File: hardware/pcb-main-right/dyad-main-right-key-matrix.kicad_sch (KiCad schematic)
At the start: 74 parts, among them SW1 SW_Push, SW10 SW_Push, SW11 SW_Push, SW12 SW_Push, SW13 SW_Push, SW14 SW_Push, SW15 SW_Push, SW16 SW_Push, SW17 SW_Push, SW18 SW_Push, SW19 SW_Push, SW2 SW_Push, SW20 SW_Push, SW21 SW_Push, SW22 SW_Push, SW23 SW_Push, SW24 SW_Push, SW25 SW_Push, SW26 SW_Push, SW27 SW_Push, SW28 SW_Push, SW29 SW_Push, SW3 SW_Push, SW30 SW_Push, SW31 SW_Push, SW32 SW_Push, SW33 SW_Push, SW34 SW_Push, SW35 SW_Push, SW36 SW_Push, SW37 SW_Push, SW4 SW_Push, SW5 SW_Push, SW6 SW_Push, SW7 SW_Push, SW8 SW_Push, SW9 SW_Push

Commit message: Move the right half's thumb keys onto their physical columns, and route it
The two rotated thumb keys were wired to COL5 and COL6 while sitting
physically leftmost on the board, because KLE puts rotated keys in their own
rows and they were numbered last. COL5 and COL6 therefore had to reach ~92 mm
across the board to find them. Relabelled 4,5 -> 4,0 and 4,6 -> 4,1 in the
KLE (with the five straight bottom-row keys shifted up to 4,2..4,6 to make
room) and regenerated: SW31 is now COL0 at x=46.23 and SW32 is COL1 at
x=68.98, both directly below the columns they belong to.

Also carries the hand routing done on top of that regeneration: all five ROW
nets and COL0-COL5, COL7 complete, 118 -> 234 segments. Unconnected 221 -> 183.
The remainder is 146 VCC/GND (no copper pours yet), 36 LED DOUT chain, and one
COL6 hop from SW22's pad to the end of its track.

Two errors on COL3 predate the routing and come from kbplacer's generated
traces: 0.1386 mm to LED26's cutout, and 0.197 mm to SW26's NPTH pad. The
nudge pass declined the first rather than mangle it -- it treats each
Edge.Cuts primitive as a separate obstacle and pushes away from that
primitive's bounding-box centre, which is meaningless for the 0.12 mm slivers
this cutout is built from. Grouping a footprint's Edge.Cuts into one obstacle
would fix it.

Co-Authored-By: Claude Opus 5 <noreply@anthropic.com>
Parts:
- SW31: footprint marbastlib-mx:SW_MX_HS_CPG151101S11_1.25u -> marbastlib-mx:SW_MX_HS_CPG151101S11_1.5u
- SW32: footprint marbastlib-mx:SW_MX_HS_CPG151101S11_1.25u -> marbastlib-mx:SW_MX_HS_CPG151101S11_1u
- SW33, SW34: footprint marbastlib-mx:SW_MX_HS_CPG151101S11_1u -> marbastlib-mx:SW_MX_HS_CPG151101S11_1.25u
- SW36: footprint marbastlib-mx:SW_MX_HS_CPG151101S11_1.5u -> marbastlib-mx:SW_MX_HS_CPG151101S11_1u

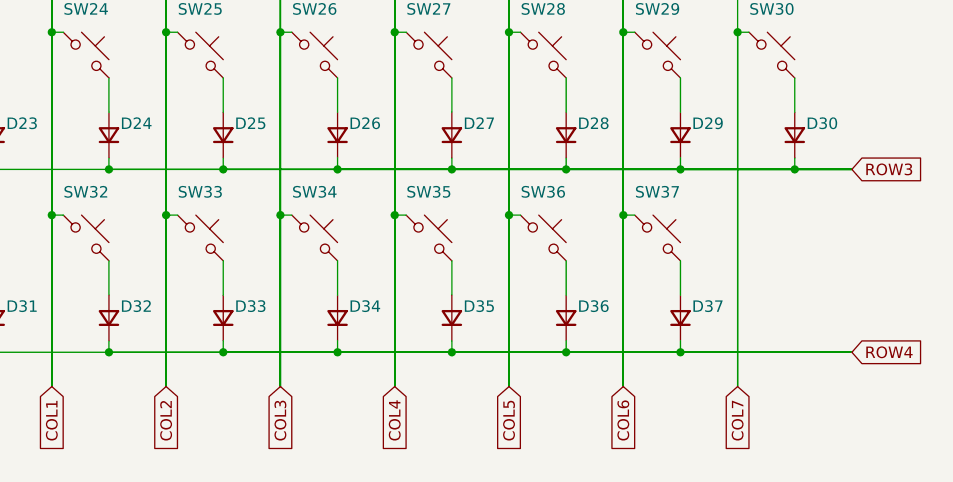
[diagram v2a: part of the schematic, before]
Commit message: Pour GND and VCC from the generator, and write down what stays manual
_add_power_pours() fills one rail per layer over the real board outline,
taken from KiCad's own outline extraction rather than reassembling the 25
Edge.Cuts segments. Pads connect solid rather than through thermal reliefs:
everything here is reflow SMD, so thermal relief buys nothing and costs the
LED rail current capacity. It also sidesteps the starved_thermal class of
error entirely.

GND goes on B.Cu, the component side. Every GND pad on these boards is
B.Cu-only, so the pour reaches all of them with no vias, and each LED's
decoupling loop to its own capacitor stays local copper rather than going
pad -> via -> plane -> via -> pad. Result: GND unconnected 0 on both halves.

VCC takes F.Cu, which carries only column traces and so gives a continuous
plane for spreading ~2 A across the LEDs. It cannot reach its pads without a
via each, and those are being added by hand -- documented rather than
generated, since via placement wants judgement about the LED/cap pairs.

  main-left    GND 12918 mm2   VCC 13646 mm2
  main-right   GND 14088 mm2   VCC 14924 mm2

Both halves regenerated, which also applies the pending bottom-row column
remap from 9b392c8. That resolved the two COL3 errors on the right -- the
0.1386 mm to LED26's cutout and 0.197 mm to SW26's NPTH pad both came from
routing that no longer exists. Every remaining error on both halves is now a
deliberate D/SW courtyard overlap.

docs/MANUAL_TASKS.md records the four things the generator cannot do: the VCC
vias, routing the rows and columns, the LED serpentine chain, and the
cosmetic silkscreen work. It carries the post-regeneration baseline numbers so
an anomaly is distinguishable from a known gap, and a "do not fix" section for
the courtyard overlaps and the 2.25u width fallback, both of which have now
been investigated twice.

Co-Authored-By: Claude Opus 5 <noreply@anthropic.com>
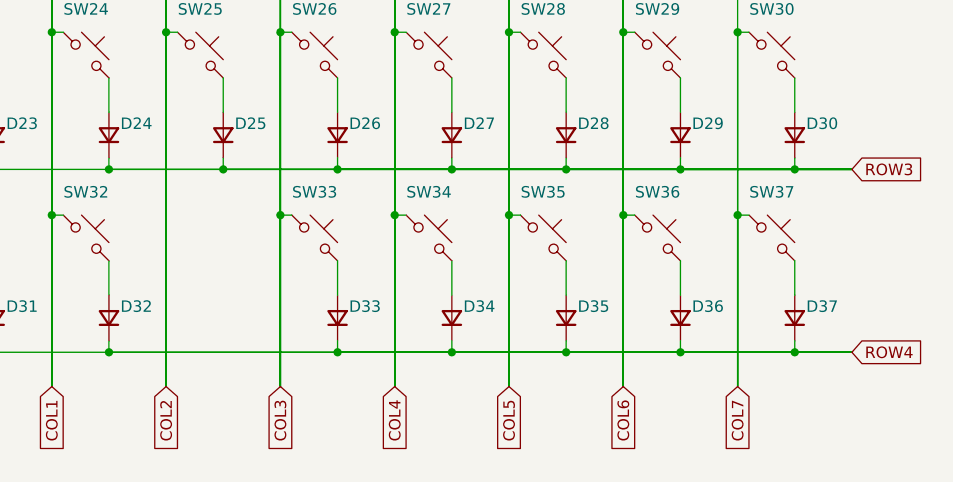
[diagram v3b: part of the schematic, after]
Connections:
- net COL2: no longer SW33.1
- net COL3: now also SW33.1; no longer SW34.1
- net COL4: now also SW34.1; no longer SW35.1
- net COL5: now also SW35.1; no longer SW36.1
- net COL6: now also SW36.1; no longer SW37.1
- net COL7: now also SW37.1

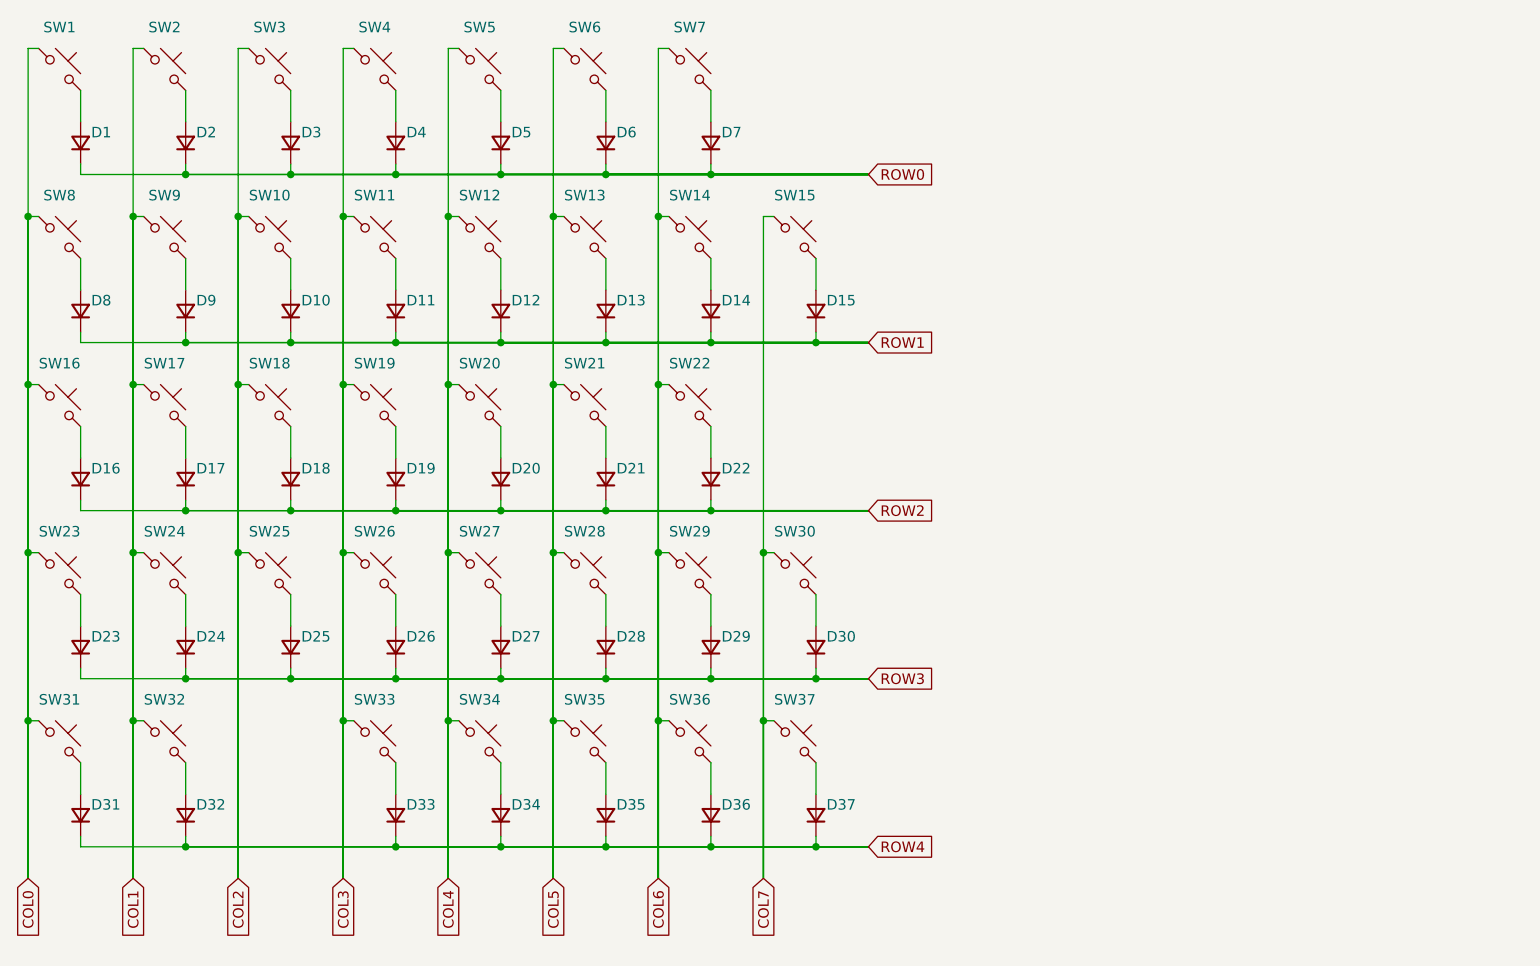
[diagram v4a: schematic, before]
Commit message: Restore the hand-drawn serpentine LED chain for the right half
I regenerated the right half without checking whether its schematics held
work that was not yet committed, and overwrote a hand-laid serpentine LED
chain. Recovered from hardware/pcb-main-right/.history, KiCad's own version
history repo, at its "SCH Save" commit a7ba379 (2026-09-15 12:59).

The led-chain sheet is byte-identical to that save: 74 symbols, 16 of them
rotated 180 degrees for the alternating rows, with every symbol repositioned
into serpentine order. All 272 wires differ from the generated version, so
this was a full re-layout rather than a rewire.

That history commit happens to postdate 2826d7a, so the bottom-row column
remap and both copper pours came back with it. The only thing missing was
the footprint linking from 2acfb55, re-applied here by calling
_link_footprints_to_symbols directly -- no kbplacer run, so nothing was
regenerated. 148/148 footprints linked.

The board still carries the old sequential chain, which is what the 31
parity findings say:

  Pad net (Net-(LEDn-DOUT)) doesn't match net given by schematic
  (Net-(LEDn-DIN))

That is the serpentine waiting to be pushed with Update PCB from Schematic,
which the footprint links now make possible. The 7 clearance and 7
solder_mask_bridge errors come from the same divergence and should go with it.

Co-Authored-By: Claude Opus 5 <noreply@anthropic.com>
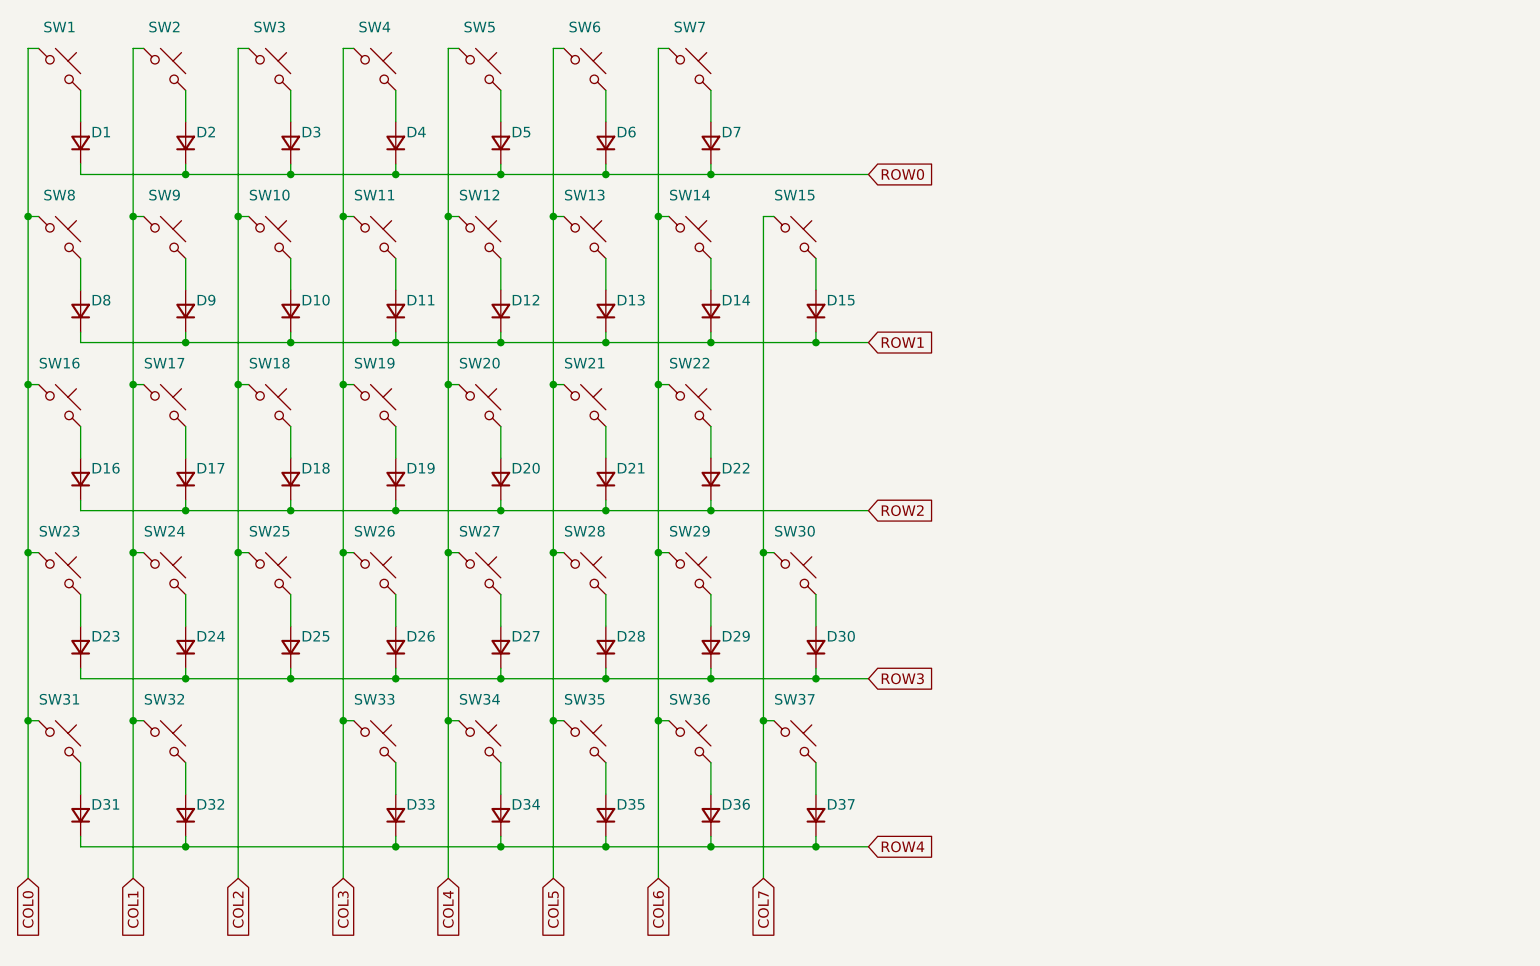
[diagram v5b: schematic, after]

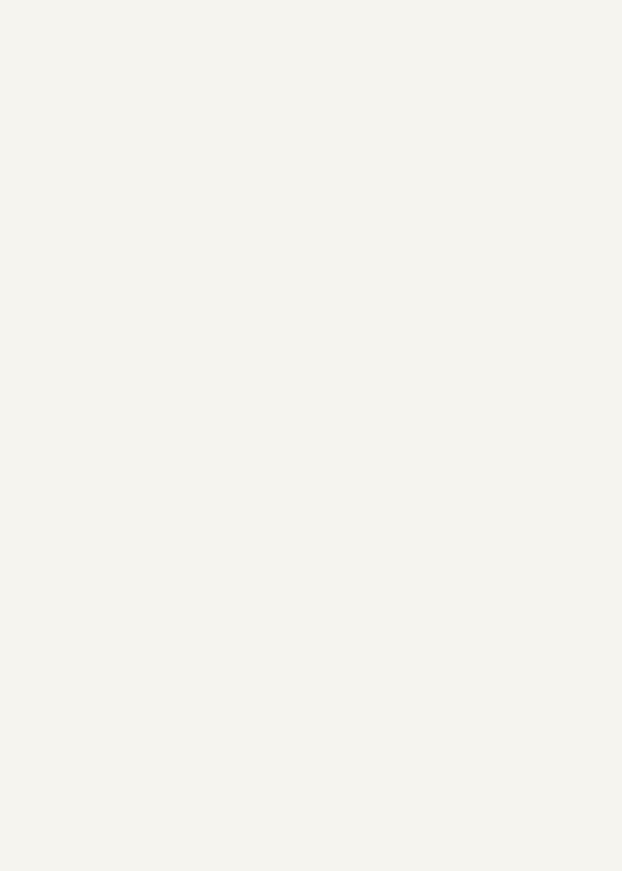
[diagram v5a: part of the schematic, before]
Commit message: Add the 20-pin FFC connector to the right half's schematic
J1 in the key-matrix sheet, Connector_Generic:Conn_01x20 against the
C19273932 footprint, with all 20 lines wired. The board can now reach the
controller as drawn.

  1,2   VCC (5 V)      11-18  COL0-7
  3,5   GND            19     +3V3
  4     LEDIN          20     HAND -> GND
  6-10  ROW4..ROW0

Rows descend where columns ascend: ascending rows forced the five row
traces to cross each other on the way to the connector. Nothing specified
the order, so this is now the order the controller and the left half must
both match.

LEDIN sits at pin 4 between the two GNDs. It is the only fast edge on the
cable and PLAN.md asks for ground returns between signals; the GNDs are the
RGB return anyway, so straddling pin 4 with them is free shielding. HAND is
pin 20 beside +3V3 at 19, which makes the left half's tie two adjacent pins
while the right half's tie is a via into the existing GND pour.

This also brings handedness and 3V3 onto the board for the first time --
the mains carried only VCC and GND. Each rail gets a PWR_FLAG, since power
arrives through a connector's passive pins.

ERC errors 3 -> 0: both power_pin_not_driven and the pin_not_driven on
LED1 DIN clear, and LEDIN is no longer an isolated label. The remaining
LEDOUT warning is correct by spec -- the chain end does not leave the board.
The 126 endpoint_off_grid warnings are untouched, which confirms every
added item is on-grid.

Co-Authored-By: Claude Opus 5 <noreply@anthropic.com>
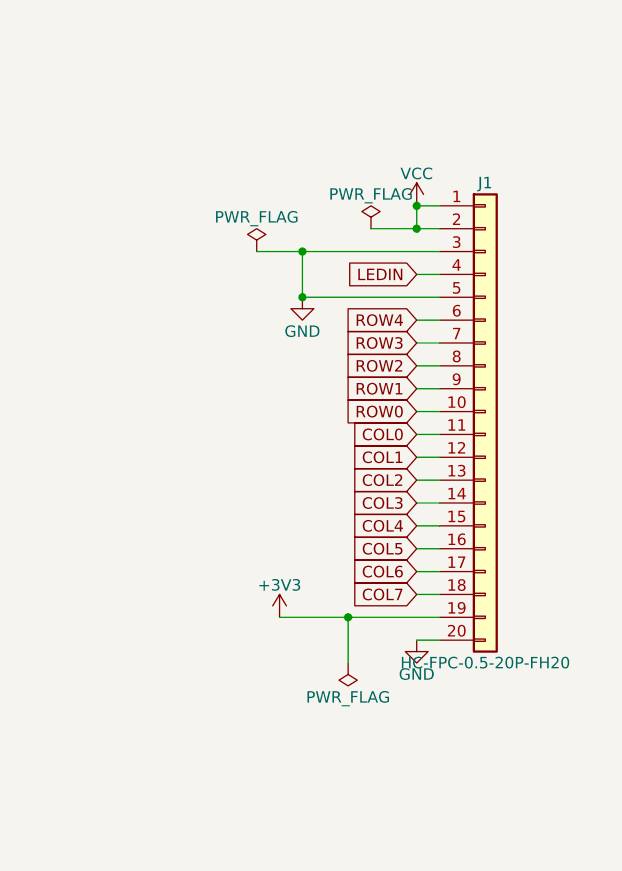
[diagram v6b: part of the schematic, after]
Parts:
- added J1: HC-FPC-0.5-20P-FH20, dyad:FPC-SMD_20P-P0.50_HC-FPC-0.5-20P-FH20, symbol Connector_Generic:Conn_01x20
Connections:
- net COL0: now also J1.11 (Pin_11)
- net COL1: now also J1.12 (Pin_12)
- net COL2: now also J1.13 (Pin_13)
- net COL3: now also J1.14 (Pin_14)
- net COL4: now also J1.15 (Pin_15)
- net COL5: now also J1.16 (Pin_16)
- net COL6: now also J1.17 (Pin_17)
- net COL7: now also J1.18 (Pin_18)
- net ROW0: now also J1.10 (Pin_10)
- net ROW1: now also J1.9 (Pin_9)
- net ROW2: now also J1.8 (Pin_8)
- net ROW3: now also J1.7 (Pin_7)
- net ROW4: now also J1.6 (Pin_6)
- new net +3V3: J1.19 (Pin_19)
- new net GND: J1.20 (Pin_20), J1.3 (Pin_3), J1.5 (Pin_5)
- new net LEDIN: J1.4 (Pin_4)
- new net VCC: J1.1 (Pin_1), J1.2 (Pin_2)
